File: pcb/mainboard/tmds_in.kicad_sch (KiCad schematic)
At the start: 31 parts, among them J4 DVI, U15 ADV7611, Y2 28.63636MHz

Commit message: r0p7 wip
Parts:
- renumbered C92 to C113, C93 to C125, C116 to C126, C119 to C127, C122 to C128, C116 to C129, C119 to C130, C122 to C131, C116 to C132, C119 to C133, C122 to C134, C116 to C135, C119 to C136, C122 to C137, C122 to C138, C119 to C139, R57 to R45, R57 to R46, R57 to R47, RN1 to RN10, RN1 to RN11, RN1 to RN12, RN1 to RN13, RN1 to RN7, RN1 to RN8, RN1 to RN9, Y2 to Y3
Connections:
- net DPI_B0: now also RN13.5 (R4.2); no longer RN13.8 (R1.2)
- net DPI_B1: now also RN13.6 (R3.2); no longer RN13.7 (R2.2)
- net DPI_B2: now also RN13.7 (R2.2); no longer RN13.6 (R3.2)
- net DPI_B3: now also RN13.8 (R1.2); no longer RN13.5 (R4.2)
- net DPI_B4: now also RN12.5 (R4.2); no longer RN12.8 (R1.2)
- net DPI_B5: now also RN12.6 (R3.2); no longer RN12.7 (R2.2)
- net DPI_B6: now also RN12.7 (R2.2); no longer RN12.6 (R3.2)
- net DPI_B7: now also RN12.8 (R1.2); no longer RN12.5 (R4.2)
- net DPI_DE: now also RN7.8 (R1.2); no longer RN7.6 (R3.2)
- net DPI_G0: now also RN8.5 (R4.2); no longer RN8.8 (R1.2)
- net DPI_G1: now also RN8.6 (R3.2); no longer RN8.7 (R2.2)
- net DPI_G2: now also RN8.7 (R2.2); no longer RN8.6 (R3.2)
- net DPI_G3: now also RN8.8 (R1.2); no longer RN8.5 (R4.2)
- net DPI_G4: now also RN9.5 (R4.2); no longer RN9.8 (R1.2)
- net DPI_G5: now also RN9.6 (R3.2); no longer RN9.7 (R2.2)
- net DPI_G6: now also RN9.7 (R2.2); no longer RN9.6 (R3.2)
- net DPI_G7: now also RN9.8 (R1.2); no longer RN9.5 (R4.2)
- net DPI_R0: now also RN11.5 (R4.2); no longer RN11.8 (R1.2)
- net DPI_R1: now also RN11.6 (R3.2); no longer RN11.7 (R2.2)
- net DPI_R2: now also RN11.7 (R2.2); no longer RN11.6 (R3.2)
- net DPI_R3: now also RN11.8 (R1.2); no longer RN11.5 (R4.2)
- net DPI_R4: now also RN10.5 (R4.2); no longer RN10.8 (R1.2)
- net DPI_R5: now also RN10.6 (R3.2); no longer RN10.7 (R2.2)
- net DPI_R6: now also RN10.7 (R2.2); no longer RN10.6 (R3.2)
- net DPI_R7: now also RN10.8 (R1.2); no longer RN10.5 (R4.2)
- net DPI_VS: now also RN7.6 (R3.2); no longer RN7.8 (R1.2)
- net at RN9.1 (R1.1): now also U15.26 (P15); no longer U15.29 (P12)
- net at RN9.2 (R2.1): now also U15.27 (P14); no longer U15.28 (P13)
- net at RN9.3 (R3.1): now also U15.28 (P13); no longer U15.27 (P14)
- net at RN9.4 (R4.1): now also U15.29 (P12); no longer U15.26 (P15)
- net at RN11.1 (R1.1): now also U15.19 (P19); no longer U15.22 (P16)
- net at RN11.2 (R2.1): now also U15.20 (P18); no longer U15.21 (P17)
- net at RN11.3 (R3.1): now also U15.21 (P17); no longer U15.20 (P18)
- net at RN11.4 (R4.1): now also U15.22 (P16); no longer U15.19 (P19)
- net at RN12.1 (R1.1): now also U15.35 (P7); no longer U15.38 (P4)
- net at RN12.2 (R2.1): now also U15.36 (P6); no longer U15.37 (P5)
- net at RN12.3 (R3.1): now also U15.37 (P5); no longer U15.36 (P6)
- net at RN12.4 (R4.1): now also U15.38 (P4); no longer U15.35 (P7)
- net at RN10.1 (R1.1): now also U15.15 (P23); no longer U15.18 (P20)
- net at RN10.2 (R2.1): now also U15.16 (P22); no longer U15.17 (P21)
- net at RN10.3 (R3.1): now also U15.17 (P21); no longer U15.16 (P22)
- net at RN10.4 (R4.1): now also U15.18 (P20); no longer U15.15 (P23)
- net at RN7.1 (R1.1): now also U15.45 (DE); no longer U15.47 (VS/FIELD/ALSB)
- net at RN7.3 (R3.1): now also U15.47 (VS/FIELD/ALSB); no longer U15.45 (DE)
- net at RN8.1 (R1.1): now also U15.30 (P11); no longer U15.33 (P8)
- net at RN8.2 (R2.1): now also U15.31 (P10); no longer U15.32 (P9)
- net at RN8.3 (R3.1): now also U15.32 (P9); no longer U15.31 (P10)
- net at RN8.4 (R4.1): now also U15.33 (P8); no longer U15.30 (P11)
- net at RN13.1 (R1.1): now also U15.39 (P3); no longer U15.43 (P0)
- net at RN13.2 (R2.1): now also U15.41 (P2); no longer U15.42 (P1)
- net at RN13.3 (R3.1): now also U15.42 (P1); no longer U15.41 (P2)
- net at RN13.4 (R4.1): now also U15.43 (P0); no longer U15.39 (P3)
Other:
- moved on the sheet: R46, RN7

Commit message: r0p7 layout done
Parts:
- J4: footprint Connector_HDMI:HDMI_Micro-D_Molex_46765-1x01 -> footprints:HDMI_Micro-D_Molex_46765-1x01_MOD
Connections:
- net ADV_P15: now reaches RN9.1 (R1.1), U15.26 (P15)
- net ADV_P14: now reaches RN9.2 (R2.1), U15.27 (P14)
- net ADV_P13: now reaches RN9.3 (R3.1), U15.28 (P13)
- net ADV_P12: now reaches RN9.4 (R4.1), U15.29 (P12)
- net ADV_P19: now reaches RN11.1 (R1.1), U15.19 (P19)
- net ADV_P18: now reaches RN11.2 (R2.1), U15.20 (P18)
- net ADV_P17: now reaches RN11.3 (R3.1), U15.21 (P17)
- net ADV_P16: now reaches RN11.4 (R4.1), U15.22 (P16)
- net ADV_P7: now reaches RN12.1 (R1.1), U15.35 (P7)
- net ADV_P6: now reaches RN12.2 (R2.1), U15.36 (P6)
- net ADV_P5: now reaches RN12.3 (R3.1), U15.37 (P5)
- net ADV_P4: now reaches RN12.4 (R4.1), U15.38 (P4)
- net ADV_P23: now reaches RN10.1 (R1.1), U15.15 (P23)
- net ADV_P22: now reaches RN10.2 (R2.1), U15.16 (P22)
- net ADV_P21: now reaches RN10.3 (R3.1), U15.17 (P21)
- net ADV_P20: now reaches RN10.4 (R4.1), U15.18 (P20)
- net ADV_DE: now reaches RN7.1 (R1.1), U15.45 (DE)
- net ADV_HS: now reaches RN7.2 (R2.1), U15.46 (HS)
- net ADV_VS: now reaches RN7.3 (R3.1), U15.47 (VS/FIELD/ALSB)
- net ADV_P11: now reaches RN8.1 (R1.1), U15.30 (P11)
- net ADV_P10: now reaches RN8.2 (R2.1), U15.31 (P10)
- net ADV_P9: now reaches RN8.3 (R3.1), U15.32 (P9)
- net ADV_P8: now reaches RN8.4 (R4.1), U15.33 (P8)
- net ADV_CK: now reaches R46.2, U15.25 (LLC)
- net ADV_P3: now reaches RN13.1 (R1.1), U15.39 (P3)
- net ADV_P2: now reaches RN13.2 (R2.1), U15.41 (P2)
- net ADV_P1: now reaches RN13.3 (R3.1), U15.42 (P1)
- net ADV_P0: now reaches RN13.4 (R4.1), U15.43 (P0)
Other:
- moved on the sheet: R46, RN10, RN11, RN12, RN13, RN7, RN8, RN9

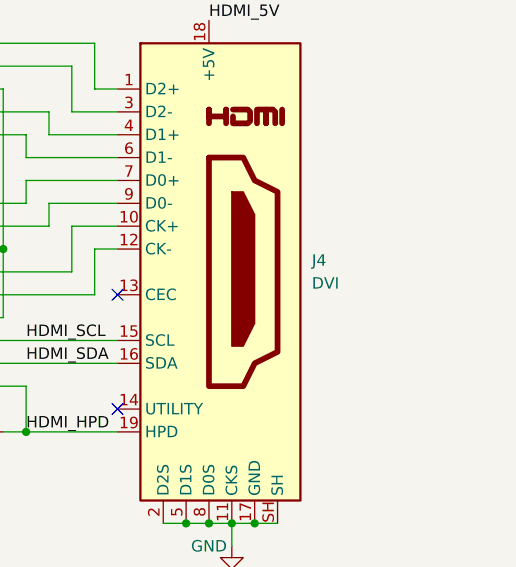
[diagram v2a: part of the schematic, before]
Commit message: Add adapter for ED067KC1/ED113TC1; revise mainboard connector model
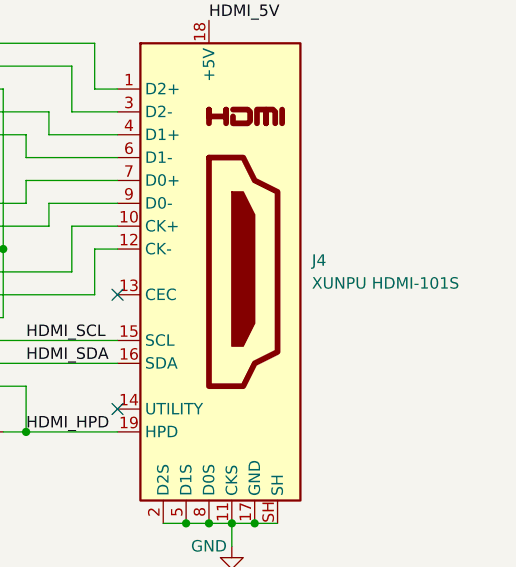
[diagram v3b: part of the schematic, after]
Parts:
- J4: value DVI -> XUNPU HDMI-101S
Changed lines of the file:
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@@
 			)
 		)
-		(property "Value" "DVI"
+		(property "Value" "XUNPU HDMI-101S"
 			(at 242.57 92.71 0)
 			(effects

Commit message: Bug fixes and changes for r0p8
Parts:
- removed J4: XUNPU HDMI-101S, footprints:HDMI_Micro-D_Molex_46765-1x01_MOD, symbol Connector:HDMI_A
- added J2: XUNPU HDMI-101S, footprints:HDMI_Micro-D_Molex_46765-1x01_MOD, symbol Connector:HDMI_D_1.4
- added R16, R49: 10K, Resistor_SMD:R_0402_1005Metric, symbol Device:R
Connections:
- net GND: now also J2.10 (D0S), J2.13 (CKS), J2.16 (GND), J2.4 (D2S), J2.7 (D1S), J2.SH
- net HDMI_5V: now also J2.19 (+5V), R16.2, R49.2
- net HDMI_HPD: now also J2.1 (HPD/HEAC-)
- net HDMI_SCL: now also J2.17 (SCL), R16.1
- net HDMI_SDA: now also J2.18 (SDA), R49.1
- net I2C_SCL: now also U15.53 (SCL); no longer U15.54 (SDA)
- net I2C_SDA: now also U15.54 (SDA); no longer U15.53 (SCL)
- net TMDS_CKN: now also J2.14 (CK-)
- net TMDS_CKP: now also J2.12 (CK+)
- net TMDS_D0N: now also J2.11 (D0-)
- net TMDS_D0P: now also J2.9 (D0+)
- net TMDS_D1N: now also J2.8 (D1-)
- net TMDS_D1P: now also J2.6 (D1+)
- net TMDS_D2N: now also J2.5 (D2-)
- net TMDS_D2P: now also J2.3 (D2+)
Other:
- company: (none) -> Copyright 2024 Wenting Zhang
- title: (none) -> Glider

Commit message: BOM adjustments
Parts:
- R46: value 33 -> 27R
- Y3: footprint Oscillator:Oscillator_SMD_Abracon_ASE-4Pin_3.2x2.5mm -> Crystal:Crystal_SMD_3225-4Pin_3.2x2.5mm
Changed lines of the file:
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@@
 			)
 		)
-		(property "Footprint" "Oscillator:Oscillator_SMD_Abracon_ASE-4Pin_3.2x2.5mm"
+		(property "Footprint" "Crystal:Crystal_SMD_3225-4Pin_3.2x2.5mm"
 			(at 185.42 130.81 0)
 			(effects
@@
 			)
 		)
-		(property "Value" "33"
+		(property "Value" "27R"
 			(at 78.74 152.8064 90)
 			(effects

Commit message: PCB r0p9
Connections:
- net ADV_DE: now also RN7.4 (R4.1); no longer RN7.1 (R1.1)
- net ADV_HS: now also RN7.3 (R3.1); no longer RN7.2 (R2.1)
- net ADV_P0: now also RN13.1 (R1.1); no longer RN13.4 (R4.1)
- net ADV_P1: now also RN13.2 (R2.1); no longer RN13.3 (R3.1)
- net ADV_P10: now also RN8.3 (R3.1); no longer RN8.2 (R2.1)
- net ADV_P11: now also RN8.4 (R4.1); no longer RN8.1 (R1.1)
- net ADV_P12: now also RN9.1 (R1.1); no longer RN9.4 (R4.1)
- net ADV_P13: now also RN9.2 (R2.1); no longer RN9.3 (R3.1)
- net ADV_P14: now also RN9.3 (R3.1); no longer RN9.2 (R2.1)
- net ADV_P15: now also RN9.4 (R4.1); no longer RN9.1 (R1.1)
- net ADV_P16: now also RN11.1 (R1.1); no longer RN11.4 (R4.1)
- net ADV_P17: now also RN11.2 (R2.1); no longer RN11.3 (R3.1)
- net ADV_P18: now also RN11.3 (R3.1); no longer RN11.2 (R2.1)
- net ADV_P19: now also RN11.4 (R4.1); no longer RN11.1 (R1.1)
- net ADV_P2: now also RN13.3 (R3.1); no longer RN13.2 (R2.1)
- net ADV_P20: now also RN10.1 (R1.1); no longer RN10.4 (R4.1)
- net ADV_P21: now also RN10.2 (R2.1); no longer RN10.3 (R3.1)
- net ADV_P22: now also RN10.3 (R3.1); no longer RN10.2 (R2.1)
- net ADV_P23: now also RN10.4 (R4.1); no longer RN10.1 (R1.1)
- net ADV_P3: now also RN13.4 (R4.1); no longer RN13.1 (R1.1)
- net ADV_P4: now also RN12.1 (R1.1); no longer RN12.4 (R4.1)
- net ADV_P5: now also RN12.2 (R2.1); no longer RN12.3 (R3.1)
- net ADV_P6: now also RN12.3 (R3.1); no longer RN12.2 (R2.1)
- net ADV_P7: now also RN12.4 (R4.1); no longer RN12.1 (R1.1)
- net ADV_P8: now also RN8.1 (R1.1); no longer RN8.4 (R4.1)
- net ADV_P9: now also RN8.2 (R2.1); no longer RN8.3 (R3.1)
- net ADV_VS: now also RN7.2 (R2.1); no longer RN7.3 (R3.1)
- net DPI_B0: now also RN13.8 (R1.2); no longer RN13.5 (R4.2)
- net DPI_B1: now also RN13.7 (R2.2); no longer RN13.6 (R3.2)
- net DPI_B2: now also RN13.6 (R3.2); no longer RN13.7 (R2.2)
- net DPI_B3: now also RN13.5 (R4.2); no longer RN13.8 (R1.2)
- net DPI_B4: now also RN12.8 (R1.2); no longer RN12.5 (R4.2)
- net DPI_B5: now also RN12.7 (R2.2); no longer RN12.6 (R3.2)
- net DPI_B6: now also RN12.6 (R3.2); no longer RN12.7 (R2.2)
- net DPI_B7: now also RN12.5 (R4.2); no longer RN12.8 (R1.2)
- net DPI_DE: now also RN7.5 (R4.2); no longer RN7.8 (R1.2)
- net DPI_G0: now also RN8.8 (R1.2); no longer RN8.5 (R4.2)
- net DPI_G1: now also RN8.7 (R2.2); no longer RN8.6 (R3.2)
- net DPI_G2: now also RN8.6 (R3.2); no longer RN8.7 (R2.2)
- net DPI_G3: now also RN8.5 (R4.2); no longer RN8.8 (R1.2)
- net DPI_G4: now also RN9.8 (R1.2); no longer RN9.5 (R4.2)
- net DPI_G5: now also RN9.7 (R2.2); no longer RN9.6 (R3.2)
- net DPI_G6: now also RN9.6 (R3.2); no longer RN9.7 (R2.2)
- net DPI_G7: now also RN9.5 (R4.2); no longer RN9.8 (R1.2)
- net DPI_HS: now also RN7.6 (R3.2); no longer RN7.7 (R2.2)
- net DPI_R0: now also RN11.8 (R1.2); no longer RN11.5 (R4.2)
- net DPI_R1: now also RN11.7 (R2.2); no longer RN11.6 (R3.2)
- net DPI_R2: now also RN11.6 (R3.2); no longer RN11.7 (R2.2)
- net DPI_R3: now also RN11.5 (R4.2); no longer RN11.8 (R1.2)
- net DPI_R4: now also RN10.8 (R1.2); no longer RN10.5 (R4.2)
- net DPI_R5: now also RN10.7 (R2.2); no longer RN10.6 (R3.2)
- net DPI_R6: now also RN10.6 (R3.2); no longer RN10.7 (R2.2)
- net DPI_R7: now also RN10.5 (R4.2); no longer RN10.8 (R1.2)
- net DPI_VS: now also RN7.7 (R2.2); no longer RN7.6 (R3.2)
- net +1V8 renamed +1V8_VID
- net +3V3 renamed +3V3_VID
- net ADV_INT: no longer names the net of U15.55 (INT1)
- net I2C_SCL renamed I2C1_SCL
- net I2C_SDA renamed I2C1_SDA
- no-connect marks 7 -> 8
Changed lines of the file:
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@@
 	)
 	(no_connect
+		(at 91.44 162.56)
+	)
+	(no_connect
 		(at 91.44 160.02)
 	)
@@
 	(wire
 		(pts
-			(xy 88.9 162.56) (xy 91.44 162.56)
-		)
-		(stroke
-			(width 0)
-			(type default)
-		)
-	)
-	(wire
-		(pts
 			(xy 142.24 66.04) (xy 137.16 66.04)
 		)
@@
 		)
 	)
-	(global_label "I2C_SCL"
+	(global_label "I2C1_SCL"
 		(shape input)
 		(at 165.1 111.76 0)
@@
 		)
 	)
-	(global_label "I2C_SDA"
+	(global_label "I2C1_SDA"
 		(shape bidirectional)
 		(at 165.1 114.3 0)
@@
 		)
 	)
-	(global_label "ADV_INT"
-		(shape output)
-		(at 88.9 162.56 180)
-		(effects
-			(font
-				(size 1.27 1.27)
-			)
-			(justify right)
-		)
-		(property "Intersheetrefs" "${INTERSHEET_REFS}"
-			(at 77.5848 162.4806 0)
-			(effects
-				(font
-					(size 1.27 1.27)
-				)
-				(justify right)
-				(hide yes)
-			)
-		)
-	)
 	(global_label "DPI_R1"
 		(shape output)
@@
 	(symbol
 		(lib_id "Device:R_Pack04")
-		(at 78.74 101.6 90)
-		(mirror x)
+		(at 78.74 99.06 90)
 		(unit 1)
 		(exclude_from_sim no)
@@
 		(dnp no)
 		(property "Reference" "RN9"
-			(at 74.93 102.87 90)
+			(at 74.93 97.79 90)
 			(effects
 				(font
@@
 		)
 		(property "Value" "33R / 4D02WGF330JTCE"
-			(at 86.36 106.68 90)
+			(at 86.36 93.98 90)
 			(effects
 				(font
@@
 		)
 		(property "Footprint" "Resistor_SMD:R_Array_Convex_4x0402"
-			(at 78.74 108.585 90)
+			(at 78.74 92.075 90)
 			(effects
 				(font
@@
 		)
 		(property "Datasheet" "~"
-			(at 78.74 101.6 0)
+			(at 78.74 99.06 0)
 			(effects
 				(font
@@
 		)
 		(property "Description" ""
-			(at 78.74 101.6 0)
+			(at 78.74 99.06 0)
 			(effects
 				(font
@@
 	(symbol
 		(lib_id "Device:R_Pack04")
-		(at 78.74 91.44 90)
-		(mirror x)
+		(at 78.74 88.9 90)
 		(unit 1)
 		(exclude_from_sim no)
@@
 		(dnp no)
 		(property "Reference" "RN11"
-			(at 74.93 92.71 90)
+			(at 74.93 87.63 90)
 			(effects
 				(font
@@
 		)
 		(property "Value" "33R / 4D02WGF330JTCE"
-			(at 86.36 81.28 90)
+			(at 86.36 99.06 90)
 			(effects
 				(font
@@
 		)
 		(property "Footprint" "Resistor_SMD:R_Array_Convex_4x0402"
-			(at 78.74 98.425 90)
+			(at 78.74 81.915 90)
 			(effects
 				(font
@@
 		)
 		(property "Datasheet" "~"
-			(at 78.74 91.44 0)
+			(at 78.74 88.9 0)
 			(effects
 				(font
@@
 		)
 		(property "Description" ""
-			(at 78.74 91.44 0)
+			(at 78.74 88.9 0)
 			(effects
 				(font
@@
 		(on_board yes)
 		(dnp no)
-		(fields_autoplaced yes)
 		(property "Reference" "#PWR0128"
 			(at 124.46 49.53 0)
@@
 			)
 		)
-		(property "Value" "+1V8"
-			(at 124.46 40.64 0)
+		(property "Value" "+1V8_VID"
+			(at 121.92 40.64 0)
 			(effects
 				(font
 					(size 1.27 1.27)
 				)
+				(justify left)
 			)
 		)
@@
 		(on_board yes)
 		(dnp no)
-		(fields_autoplaced yes)
 		(property "Reference" "#PWR0127"
 			(at 119.38 49.53 0)
@@
 			)
 		)
-		(property "Value" "+3V3"
-			(at 119.38 40.64 0)
+		(property "Value" "+3V3_VID"
+			(at 111.76 40.64 0)
 			(effects
 				(font
 					(size 1.27 1.27)
 				)
+				(justify left)
 			)
 		)
@@
 	(symbol
 		(lib_id "Device:R_Pack04")
-		(at 78.74 121.92 90)
-		(mirror x)
+		(at 78.74 119.38 90)
 		(unit 1)
 		(exclude_from_sim no)
@@
 		(dnp no)
 		(property "Reference" "RN12"
-			(at 74.93 123.19 90)
+			(at 74.93 118.11 90)
 			(effects
 				(font
@@
 		)
 		(property "Value" "33R / 4D02WGF330JTCE"
-			(at 86.36 127 90)
+			(at 86.36 114.3 90)
 			(effects
 				(font
@@
 		)
 		(property "Footprint" "Resistor_SMD:R_Array_Convex_4x0402"
-			(at 78.74 128.905 90)
+			(at 78.74 112.395 90)
 			(effects
 				(font
@@
 		)
 		(property "Datasheet" "~"
-			(at 78.74 121.92 0)
+			(at 78.74 119.38 0)
 			(effects
 				(font
@@
 		)
 		(property "Description" ""
-			(at 78.74 121.92 0)
+			(at 78.74 119.38 0)
 			(effects
 				(font
@@
 	(symbol
 		(lib_id "Device:R_Pack04")
-		(at 78.74 81.28 90)
-		(mirror x)
+		(at 78.74 78.74 90)
 		(unit 1)
 		(exclude_from_sim no)
@@
 		(dnp no)
 		(property "Reference" "RN10"
-			(at 74.93 82.55 90)
+			(at 74.93 77.47 90)
 			(effects
 				(font
@@
 		)
 		(property "Value" "33R / 4D02WGF330JTCE"
-			(at 86.36 86.36 90)
+			(at 86.36 73.66 90)
 			(effects
 				(font
@@
 		)
 		(property "Footprint" "Resistor_SMD:R_Array_Convex_4x0402"
-			(at 78.74 88.265 90)
+			(at 78.74 71.755 90)
 			(effects
 				(font
@@
 		)
 		(property "Datasheet" "~"
-			(at 78.74 81.28 0)
+			(at 78.74 78.74 0)
 			(effects
 				(font
@@
 		)
 		(property "Description" ""
-			(at 78.74 81.28 0)
+			(at 78.74 78.74 0)
 			(effects
 				(font
@@
 	(symbol
 		(lib_id "Device:R_Pack04")
-		(at 78.74 144.78 90)
-		(mirror x)
+		(at 78.74 142.24 90)
 		(unit 1)
 		(exclude_from_sim no)
@@
 		(dnp no)
 		(property "Reference" "RN7"
-			(at 74.93 146.05 90)
+			(at 74.93 140.97 90)
 			(effects
 				(font
@@
 		)
 		(property "Value" "33R / 4D02WGF330JTCE"
-			(at 87.503 143.2052 90)
+			(at 87.503 143.8148 90)
 			(effects
 				(font
@@
 		)
 		(property "Footprint" "Resistor_SMD:R_Array_Convex_4x0402"
-			(at 78.74 151.765 90)
+			(at 78.74 135.255 90)
 			(effects
 				(font
@@
 		)
 		(property "Datasheet" "~"
-			(at 78.74 144.78 0)
+			(at 78.74 142.24 0)
 			(effects
 				(font
@@
 		)
 		(property "Description" ""
-			(at 78.74 144.78 0)
+			(at 78.74 142.24 0)
 			(effects
 				(font
@@
 	(symbol
 		(lib_id "Device:R_Pack04")
-		(at 78.74 111.76 90)
-		(mirror x)
+		(at 78.74 109.22 90)
 		(unit 1)
 		(exclude_from_sim no)
@@
 		(dnp no)
 		(property "Reference" "RN8"
-			(at 74.93 113.03 90)
+			(at 74.93 107.95 90)
 			(effects
 				(font
@@
 		)
 		(property "Value" "33R / 4D02WGF330JTCE"
-			(at 86.36 101.6 90)
+			(at 86.36 119.38 90)
 			(effects
 				(font
@@
 		)
 		(property "Footprint" "Resistor_SMD:R_Array_Convex_4x0402"
-			(at 78.74 118.745 90)
+			(at 78.74 102.235 90)
 			(effects
 				(font
@@
 		)
 		(property "Datasheet" "~"
-			(at 78.74 111.76 0)
+			(at 78.74 109.22 0)
 			(effects
 				(font
@@
 		)
 		(property "Description" ""
-			(at 78.74 111.76 0)
+			(at 78.74 109.22 0)
 			(effects
 				(font
@@
 	(symbol
 		(lib_id "Device:R_Pack04")
-		(at 78.74 132.08 90)
-		(mirror x)
+		(at 78.74 129.54 90)
 		(unit 1)
 		(exclude_from_sim no)
@@
 		(dnp no)
 		(property "Reference" "RN13"
-			(at 74.93 133.35 90)
+			(at 74.93 128.27 90)
 			(effects
 				(font
@@
 		)
 		(property "Value" "33R / 4D02WGF330JTCE"
-			(at 86.36 121.92 90)
+			(at 86.36 139.7 90)
 			(effects
 				(font
@@
 		)
 		(property "Footprint" "Resistor_SMD:R_Array_Convex_4x0402"
-			(at 78.74 139.065 90)
+			(at 78.74 122.555 90)
 			(effects
 				(font
@@
 		)
 		(property "Datasheet" "~"
-			(at 78.74 132.08 0)
+			(at 78.74 129.54 0)
 			(effects
 				(font
@@
 		)
 		(property "Description" ""
-			(at 78.74 132.08 0)
+			(at 78.74 129.54 0)
 			(effects
 				(font
